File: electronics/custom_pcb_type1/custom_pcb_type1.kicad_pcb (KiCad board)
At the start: 2 copper layers, 100.3 x 69.8 mm, 25 parts, among them J1 BELT_CONN_1, J2 BELT_CONN_2, J3 SEN0140, J4 USB_B, J5 JMPR_TO_ATMEGA, Q1 2N2222, Q2 2N2222, Q3 2N2222, Q4 2N2222, Q5 2N2222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

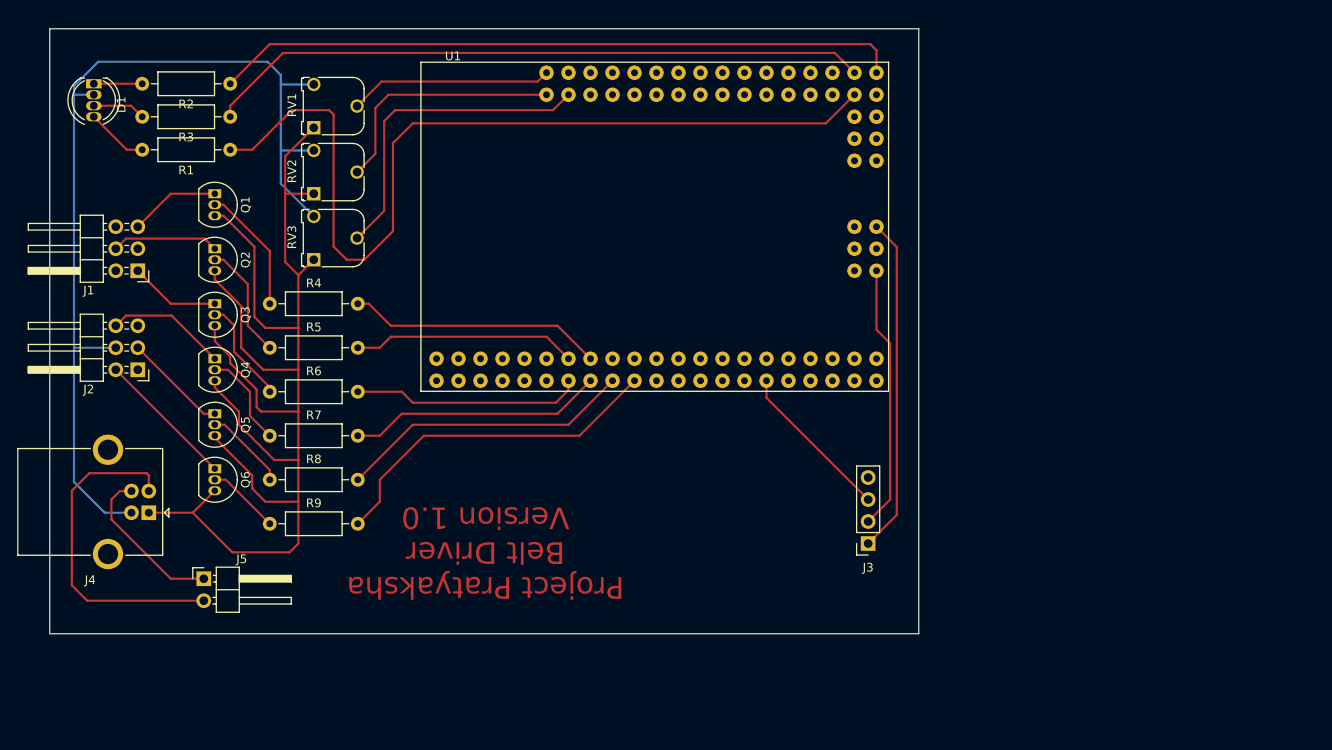
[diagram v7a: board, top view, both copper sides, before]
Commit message: Rerouting to be single-sided
Since I can't plate my through-holes, any connections on the opposite side of the board had to be soldered too. The problem there is that the components are in the way so you can't solder. Because of this I decided to route all the ground traces on the top. At first I had planned to just put some through-hole vias that were away from components to fix that soldering issue. Then I realized I could route them all on the top no problem, so I went that way. The traces are really the "bottom" now and the top is where the components are with the project name/version mask.

Also didn't realize I forgot to connect one of the pins for the SEN0140 board. I guess I deleted the trace with the intent to reroute it but never did. Fixed now.

Finally, all my hard work with the last board was for nothing in the end as I had my print settings at the default. Apparently microsoft edge defaults to printing everything scaled instead of 100%. Got all finished drilling the holes by hand with a pin vice and then found the headers wouldnt line up. ggwp git gud. :(
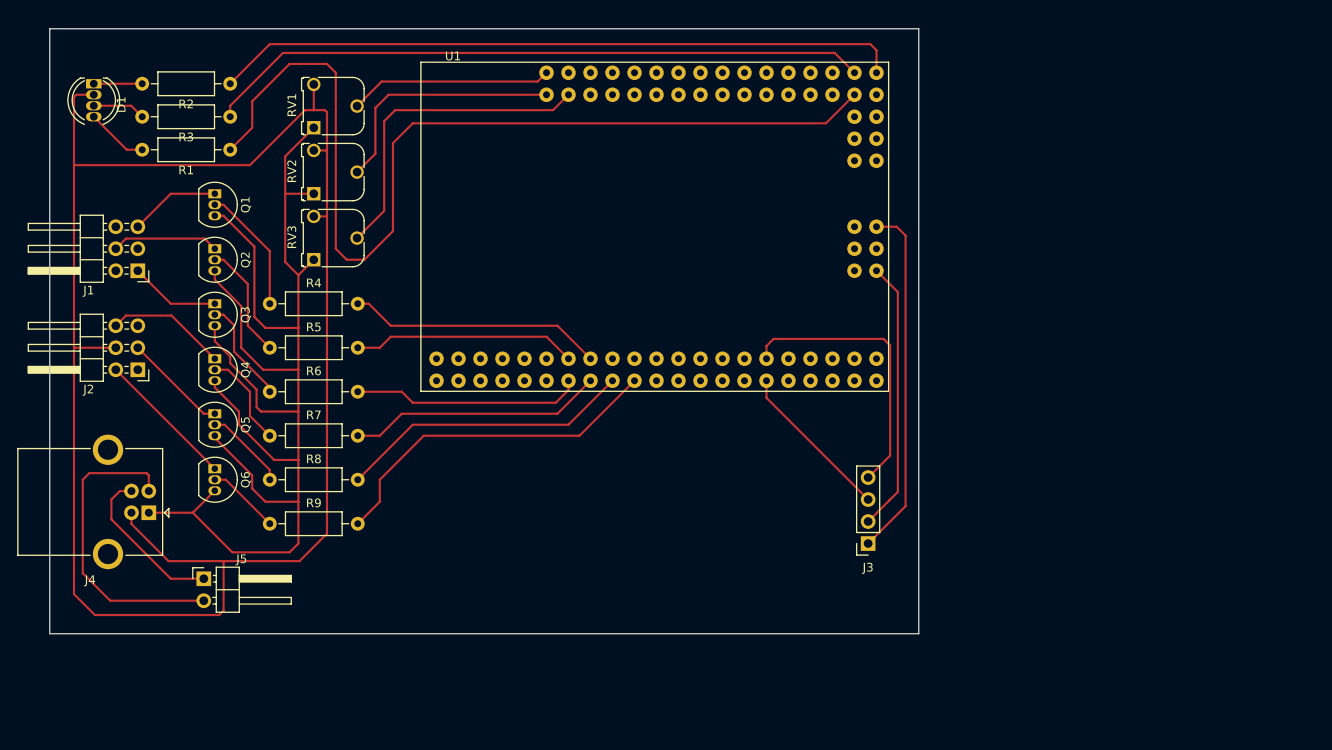
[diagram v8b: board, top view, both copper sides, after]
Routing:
- net GND: track 112.2 -> 202.9 mm
- net Net-(J3-Pad4): track 0.00 -> 32.7 mm
- net Net-(R1-Pad1): track 103.9 -> 113.1 mm
- net Net-(J4-Pad2): track 38.6 -> 35.9 mm
- net Net-(J3-Pad1): track 38.9 -> 41.1 mm
- net Net-(J3-Pad2): track 30.7 -> 31.6 mm
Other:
- rule trace_min: 0.6 -> 0.2
- board text added: "Project Pratyaksha Belt Driver Version 1.1"
- board text removed: "Project Pratyaksha Belt Driver Version 1.0"
